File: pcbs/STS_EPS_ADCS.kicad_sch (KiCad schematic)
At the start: 20 parts, among them U10 MAX11632EEGT, U5 MAX11632EEGT, U6 MAX11632EEGT, U7 MAX11632EEGT, U8 MAX11632EEGT, U9 MAX11632EEGT

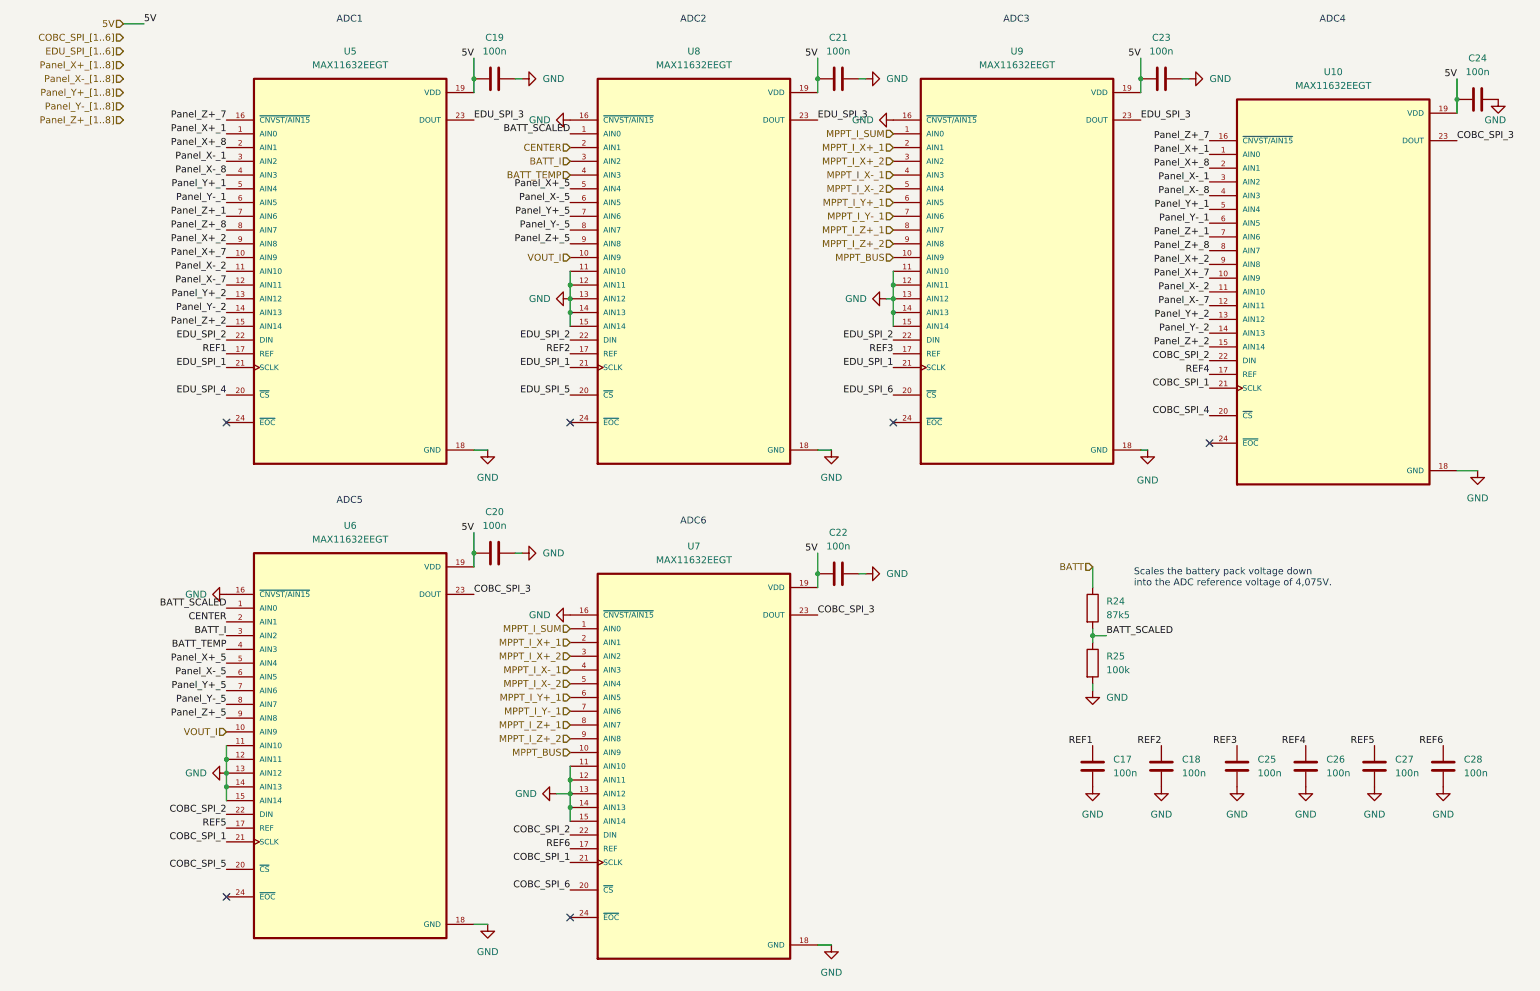
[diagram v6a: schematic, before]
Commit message: Worked on STS1_EPS_1.
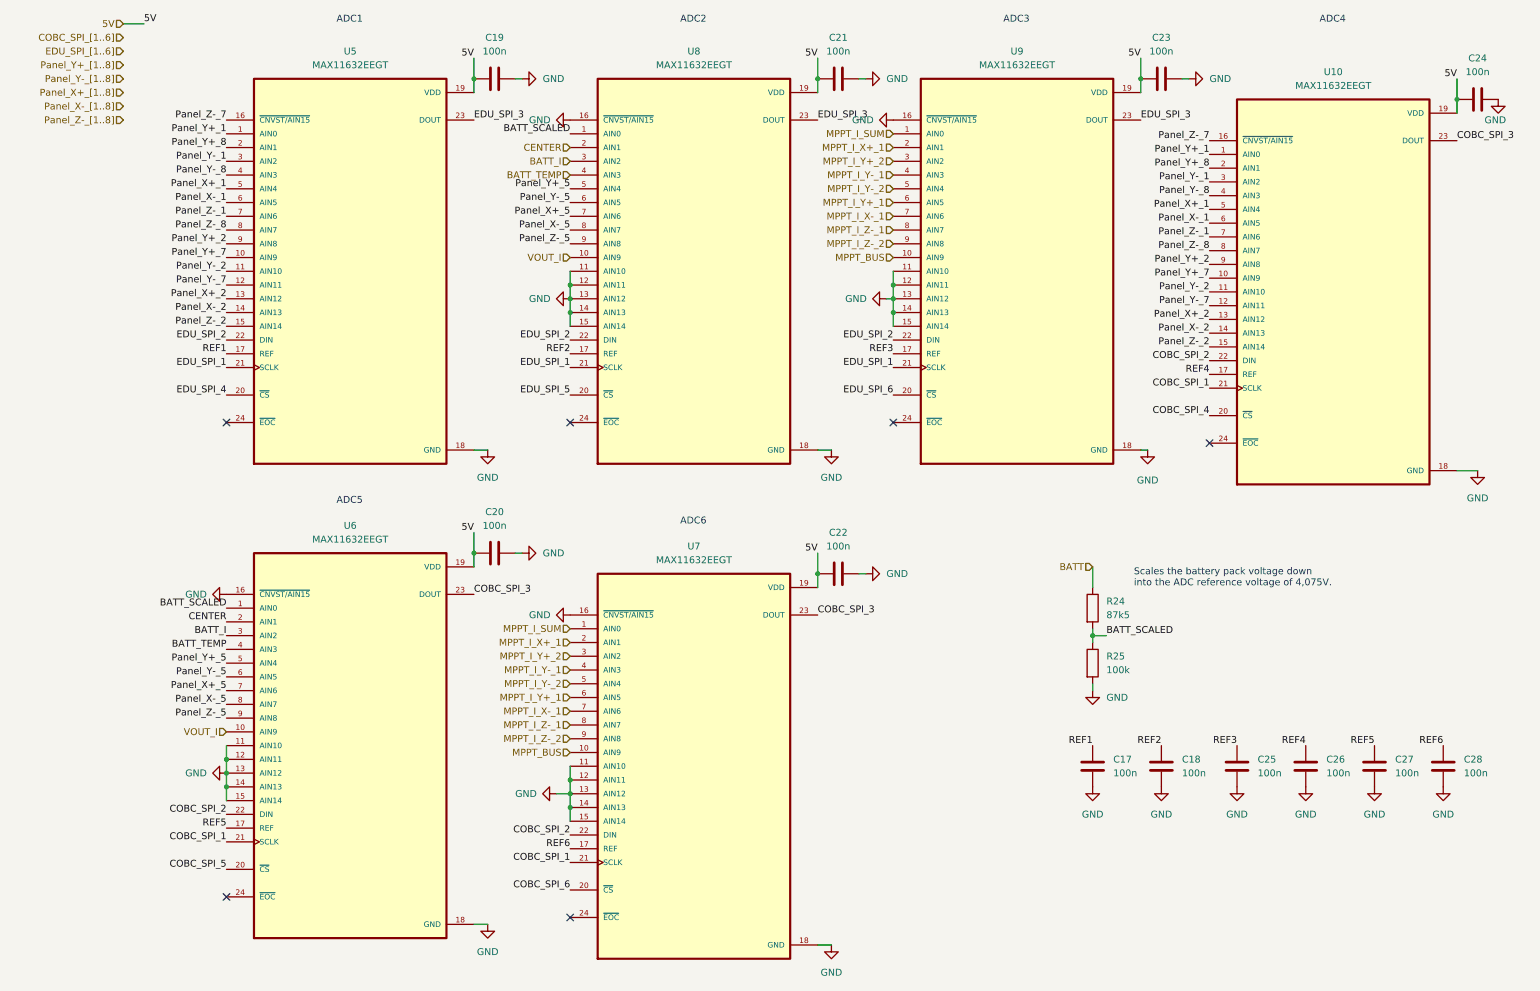
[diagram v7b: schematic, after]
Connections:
- net MPPT_I_X-_1: now also U7.7 (AIN6), U9.7 (AIN6); no longer U7.4 (AIN3), U9.4 (AIN3)
- net MPPT_I_Y-_1: now also U7.4 (AIN3), U9.4 (AIN3); no longer U7.7 (AIN6), U9.7 (AIN6)
- net Panel_X+_1: now also U10.5 (AIN4), U5.5 (AIN4); no longer U10.1 (AIN0), U5.1 (AIN0)
- net Panel_X+_2: now also U10.13 (AIN12), U5.13 (AIN12); no longer U10.9 (AIN8), U5.9 (AIN8)
- net Panel_X+_5: now also U6.7 (AIN6), U8.7 (AIN6); no longer U6.5 (AIN4), U8.5 (AIN4)
- net Panel_X-_1: now also U10.6 (AIN5), U5.6 (AIN5); no longer U10.3 (AIN2), U5.3 (AIN2)
- net Panel_X-_2: now also U10.14 (AIN13), U5.14 (AIN13); no longer U10.11 (AIN10), U5.11 (AIN10)
- net Panel_X-_5: now also U6.8 (AIN7), U8.8 (AIN7); no longer U6.6 (AIN5), U8.6 (AIN5)
- net Panel_Y+_1: now also U10.1 (AIN0), U5.1 (AIN0); no longer U10.5 (AIN4), U5.5 (AIN4)
- net Panel_Y+_2: now also U10.9 (AIN8), U5.9 (AIN8); no longer U10.13 (AIN12), U5.13 (AIN12)
- net Panel_Y+_5: now also U6.5 (AIN4), U8.5 (AIN4); no longer U6.7 (AIN6), U8.7 (AIN6)
- net Panel_Y-_1: now also U10.3 (AIN2), U5.3 (AIN2); no longer U10.6 (AIN5), U5.6 (AIN5)
- net Panel_Y-_2: now also U10.11 (AIN10), U5.11 (AIN10); no longer U10.14 (AIN13), U5.14 (AIN13)
- net Panel_Y-_5: now also U6.6 (AIN5), U8.6 (AIN5); no longer U6.8 (AIN7), U8.8 (AIN7)
- net MPPT_I_X+_2 renamed MPPT_I_Y+_2
- net MPPT_I_X-_2 renamed MPPT_I_Y-_2
- net MPPT_I_Z+_1 renamed MPPT_I_Z-_1
- net MPPT_I_Z+_2 renamed MPPT_I_Z-_2
- net Panel_X+_7 renamed Panel_Y+_7
- net Panel_X+_8 renamed Panel_Y+_8
- net Panel_X-_7 renamed Panel_Y-_7
- net Panel_X-_8 renamed Panel_Y-_8
- net Panel_Z+_1 renamed Panel_Z-_1
- net Panel_Z+_2 renamed Panel_Z-_2
- net Panel_Z+_5 renamed Panel_Z-_5
- net Panel_Z+_7 renamed Panel_Z-_7
- net Panel_Z+_8 renamed Panel_Z-_8

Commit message: Worked on STS1_EPS_1.
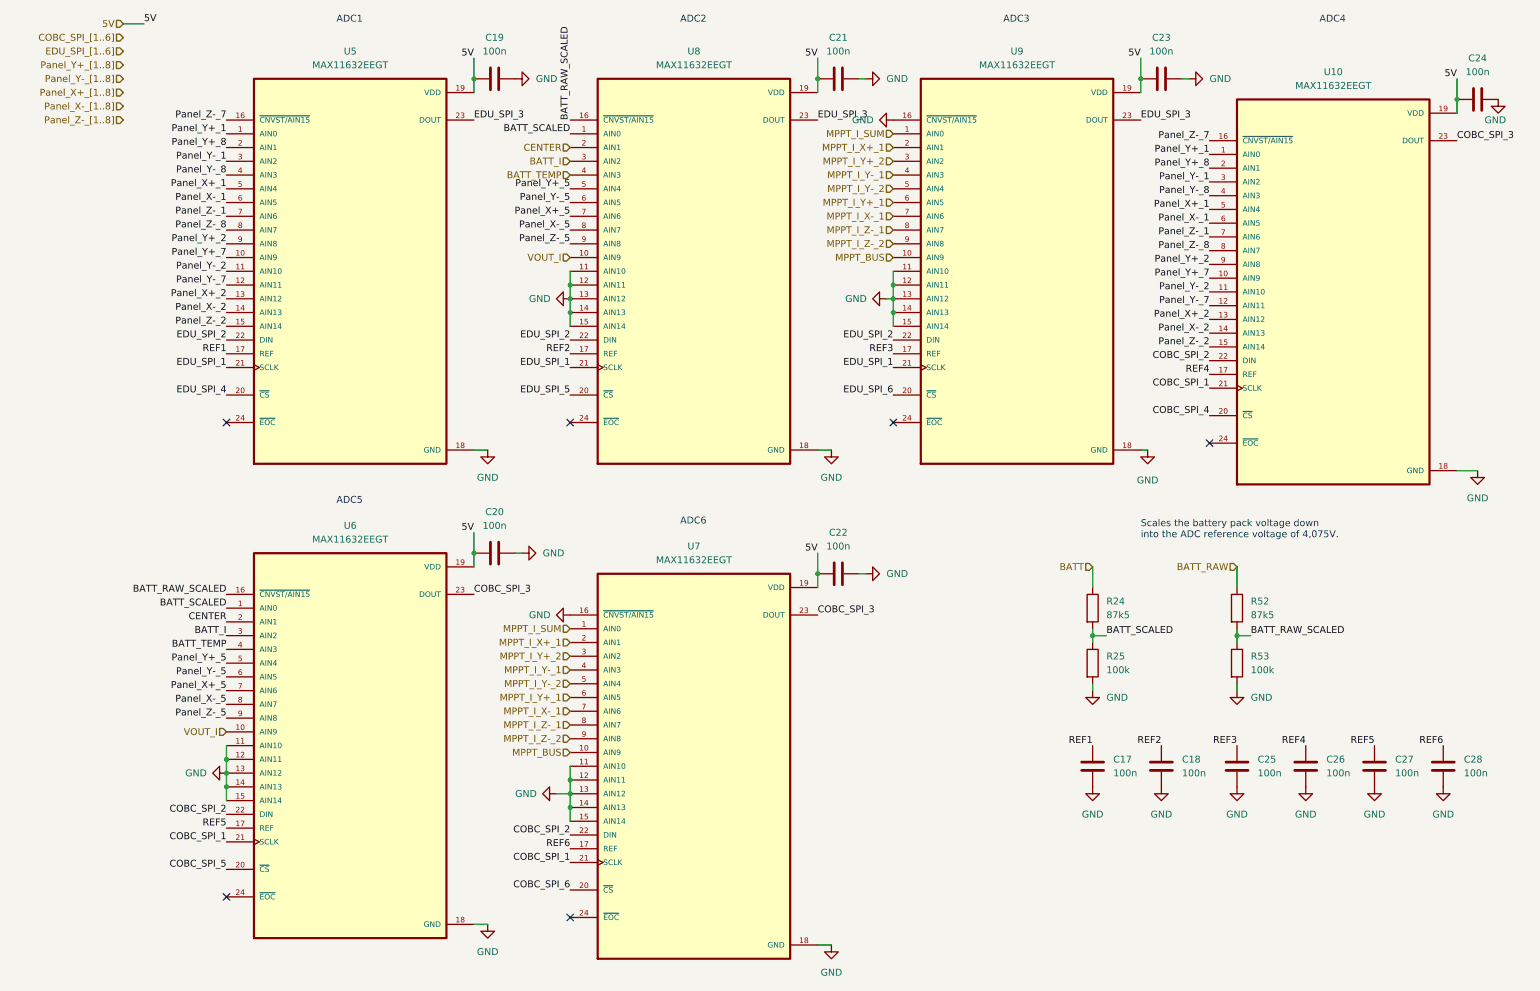
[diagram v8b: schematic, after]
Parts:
- added R52: 87k5, Resistor_SMD:R_0805_2012Metric, symbol Device:R
- added R53: 100k, Resistor_SMD:R_0805_2012Metric, symbol Device:R
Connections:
- net GND: now also R53.2; no longer U6.16 (~{CNVST/AIN15}), U8.16 (~{CNVST/AIN15})
- new net BATT_RAW: R52.1
- new net BATT_RAW_SCALED: R52.2, R53.1, U6.16 (~{CNVST/AIN15}), U8.16 (~{CNVST/AIN15})
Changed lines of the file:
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@@
   (junction (at 111.76 158.75) (diameter 0) (color 0 0 0 0)
+  )
+  (junction (at 234.95 129.54) (diameter 0) (color 0 0 0 0)
   )
   (junction (at 171.45 67.31) (diameter 0) (color 0 0 0 0)
@@
     (stroke (width 0) (type default) (color 0 0 0 0))
   )
+  (wire (pts (xy 234.95 128.27) (xy 234.95 129.54))
+    (stroke (width 0) (type default) (color 0 0 0 0))
+  )
   (wire (pts (xy 171.45 64.77) (xy 171.45 67.31))
     (stroke (width 0) (type default) (color 0 0 0 0))
@@
     (stroke (width 0) (type default) (color 0 0 0 0))
   )
+  (wire (pts (xy 234.95 129.54) (xy 234.95 130.81))
+    (stroke (width 0) (type default) (color 0 0 0 0))
+  )
   (wire (pts (xy 93.98 22.86) (xy 93.98 26.67))
     (stroke (width 0) (type default) (color 0 0 0 0))
@@
     (stroke (width 0) (type default) (color 0 0 0 0))
   )
+  (wire (pts (xy 234.95 138.43) (xy 234.95 139.7))
+    (stroke (width 0) (type default) (color 0 0 0 0))
+  )
   (wire (pts (xy 48.26 157.48) (xy 48.26 160.02))
     (stroke (width 0) (type default) (color 0 0 0 0))
@@
     (stroke (width 0) (type default) (color 0 0 0 0))
   )
+  (wire (pts (xy 234.95 129.54) (xy 237.49 129.54))
+    (stroke (width 0) (type default) (color 0 0 0 0))
+  )
   (wire (pts (xy 157.48 186.69) (xy 160.02 186.69))
     (stroke (width 0) (type default) (color 0 0 0 0))
@@
     (stroke (width 0) (type default) (color 0 0 0 0))
   )
-  (wire (pts (xy 101.6 26.67) (xy 102.87 26.67))
-    (stroke (width 0) (type default) (color 0 0 0 0))
-  )
   (wire (pts (xy 48.26 152.4) (xy 48.26 154.94))
     (stroke (width 0) (type default) (color 0 0 0 0))
@@
     (stroke (width 0) (type default) (color 0 0 0 0))
   )
+  (wire (pts (xy 234.95 116.84) (xy 234.95 120.65))
+    (stroke (width 0) (type default) (color 0 0 0 0))
+  )
   (wire (pts (xy 111.76 156.21) (xy 111.76 158.75))
     (stroke (width 0) (type default) (color 0 0 0 0))
@@
   )
   (text "Scales the battery pack voltage down \ninto the ADC reference voltage of 4,075V."
-    (at 215.9 120.65 0)
+    (at 217.17 111.76 0)
     (effects (font (size 1.27 1.27)) (justify left bottom))
   )
@@
     (effects (font (size 1.27 1.27)) (justify right bottom))
   )
+  (label "BATT_RAW_SCALED" (at 111.76 34.29 90)
+    (effects (font (size 1.27 1.27)) (justify left bottom))
+  )
   (label "Panel_X-_2" (at 48.26 69.85 180)
     (effects (font (size 1.27 1.27)) (justify right bottom))
@@
     (effects (font (size 1.27 1.27)) (justify right bottom))
   )
+  (label "BATT_RAW_SCALED" (at 237.49 129.54 0)
+    (effects (font (size 1.27 1.27)) (justify left bottom))
+  )
   (label "COBC_SPI_5" (at 48.26 172.72 180)
     (effects (font (size 1.27 1.27)) (justify right bottom))
@@
     (effects (font (size 1.27 1.27)) (justify right bottom))
   )
+  (label "BATT_RAW_SCALED" (at 48.26 121.92 180)
+    (effects (font (size 1.27 1.27)) (justify right bottom))
+  )
   (label "Panel_Z-_8" (at 48.26 54.61 180)
     (effects (font (size 1.27 1.27)) (justify right bottom))
@@
   )
   (hierarchical_label "MPPT_I_Z-_1" (shape input) (at 111.76 146.05 180)
+    (effects (font (size 1.27 1.27)) (justify right))
+  )
+  (hierarchical_label "BATT_RAW" (shape input) (at 234.95 116.84 180)
     (effects (font (size 1.27 1.27)) (justify right))
   )
@@
     (pin "1")
   )
+  (symbol (lib_id "power:GND") (at 234.95 139.7 0) (unit 1)
+    (in_bom yes) (on_board yes) (fields_autoplaced)
+    (property "Reference" "#PWR070" (id 0) (at 234.95 146.05 0)
+      (effects (font (size 1.27 1.27)) hide)
+    )
+    (property "Value" "GND" (id 1) (at 237.49 140.9699 0)
+      (effects (font (size 1.27 1.27)) (justify left))
+    )
+    (property "Footprint" "" (id 2) (at 234.95 139.7 0)
+      (effects (font (size 1.27 1.27)) hide)
+    )
+    (property "Datasheet" "" (id 3) (at 234.95 139.7 0)
+      (effects (font (size 1.27 1.27)) hide)
+    )
+    (pin "1")
+  )
   (symbol (lib_id "power:GND") (at 226.06 26.67 90) (unit 1)
     (in_bom yes) (on_board yes) (fields_autoplaced)
@@
     (pin "1")
   )
+  (symbol (lib_id "Device:R") (at 234.95 134.62 0) (unit 1)
+    (in_bom yes) (on_board yes) (fields_autoplaced)
+    (property "Reference" "R53" (id 0) (at 237.49 133.3499 0)
+      (effects (font (size 1.27 1.27)) (justify left))
+    )
+    (property "Value" "100k" (id 1) (at 237.49 135.8899 0)
+      (effects (font (size 1.27 1.27)) (justify left))
+    )
+    (property "Footprint" "Resistor_SMD:R_0805_2012Metric" (id 2) (at 233.172 134.62 90)
+      (effects (font (size 1.27 1.27)) hide)
+    )
+    (property "Datasheet" "~" (id 3) (at 234.95 134.62 0)
+      (effects (font (size 1.27 1.27)) hide)
+    )
+    (pin "1")
+    (pin "2")
+  )
   (symbol (lib_id "Device:C") (at 208.28 153.67 180) (unit 1)
     (in_bom yes) (on_board yes) (fields_autoplaced)
@@
     (pin "1")
   )
-  (symbol (lib_id "power:GND") (at 48.26 121.92 270) (unit 1)
-    (in_bom yes) (on_board yes)
-    (property "Reference" "#PWR068" (id 0) (at 41.91 121.92 0)
-      (effects (font (size 1.27 1.27)) hide)
-    )
-    (property "Value" "GND" (id 1) (at 40.64 121.92 90)
-      (effects (font (size 1.27 1.27)) (justify left))
-    )
-    (property "Footprint" "" (id 2) (at 48.26 121.92 0)
-      (effects (font (size 1.27 1.27)) hide)
-    )
-    (property "Datasheet" "" (id 3) (at 48.26 121.92 0)
-      (effects (font (size 1.27 1.27)) hide)
-    )
-    (pin "1")
-  )
   (symbol (lib_id "power:GND") (at 102.87 114.3 90) (unit 1)
     (in_bom yes) (on_board yes) (fields_autoplaced)
@@
     (pin "2")
   )
-  (symbol (lib_id "power:GND") (at 111.76 34.29 270) (unit 1)
-    (in_bom yes) (on_board yes)
-    (property "Reference" "#PWR070" (id 0) (at 105.41 34.29 0)
-      (effects (font (size 1.27 1.27)) hide)
-    )
-    (property "Value" "GND" (id 1) (at 104.14 34.29 90)
-      (effects (font (size 1.27 1.27)) (justify left))
-    )
-    (property "Footprint" "" (id 2) (at 111.76 34.29 0)
-      (effects (font (size 1.27 1.27)) hide)
-    )
-    (property "Datasheet" "" (id 3) (at 111.76 34.29 0)
-      (effects (font (size 1.27 1.27)) hide)
-    )
-    (pin "1")
-  )
-  (symbol (lib_id "power:GND") (at 102.87 26.67 90) (unit 1)
-    (in_bom yes) (on_board yes) (fields_autoplaced)
-    (property "Reference" "#PWR057" (id 0) (at 109.22 26.67 0)
-      (effects (font (size 1.27 1.27)) hide)
-    )
-    (property "Value" "GND" (id 1) (at 106.68 26.6699 90)
-      (effects (font (size 1.27 1.27)) (justify right))
-    )
-    (property "Footprint" "" (id 2) (at 102.87 26.67 0)
-      (effects (font (size 1.27 1.27)) hide)
-    )
-    (property "Datasheet" "" (id 3) (at 102.87 26.67 0)
+  (symbol (lib_id "power:GND") (at 101.6 26.67 90) (unit 1)
+    (in_bom yes) (on_board yes) (fields_autoplaced)
+    (property "Reference" "#PWR057" (id 0) (at 107.95 26.67 0)
+      (effects (font (size 1.27 1.27)) hide)
+    )
+    (property "Value" "GND" (id 1) (at 105.41 26.6699 90)
+      (effects (font (size 1.27 1.27)) (justify right))
+    )
+    (property "Footprint" "" (id 2) (at 101.6 26.67 0)
+      (effects (font (size 1.27 1.27)) hide)
+    )
+    (property "Datasheet" "" (id 3) (at 101.6 26.67 0)
       (effects (font (size 1.27 1.27)) hide)
     )
@@
       (effects (font (size 1.27 1.27)) hide)
     )
+    (pin "1")
+    (pin "2")
+  )
+  (symbol (lib_id "Device:R") (at 234.95 124.46 0) (unit 1)
+    (in_bom yes) (on_board yes) (fields_autoplaced)
+    (property "Reference" "R52" (id 0) (at 237.49 123.1899 0)
+      (effects (font (size 1.27 1.27)) (justify left))
+    )
+    (property "Value" "87k5" (id 1) (at 237.49 125.7299 0)
+      (effects (font (size 1.27 1.27)) (justify left))
+    )
+    (property "Footprint" "Resistor_SMD:R_0805_2012Metric" (id 2) (at 233.172 124.46 90)
+      (effects (font (size 1.27 1.27)) hide)
+    )
+    (property "Datasheet" "~" (id 3) (at 234.95 124.46 0)
+      (effects (font (size 1.27 1.27)) hide)
+    )
